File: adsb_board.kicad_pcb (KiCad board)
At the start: 2 copper layers, 3 parts, among them J1 Conn_Coaxial, J2 Conn_Coaxial, U1 TA1090EC

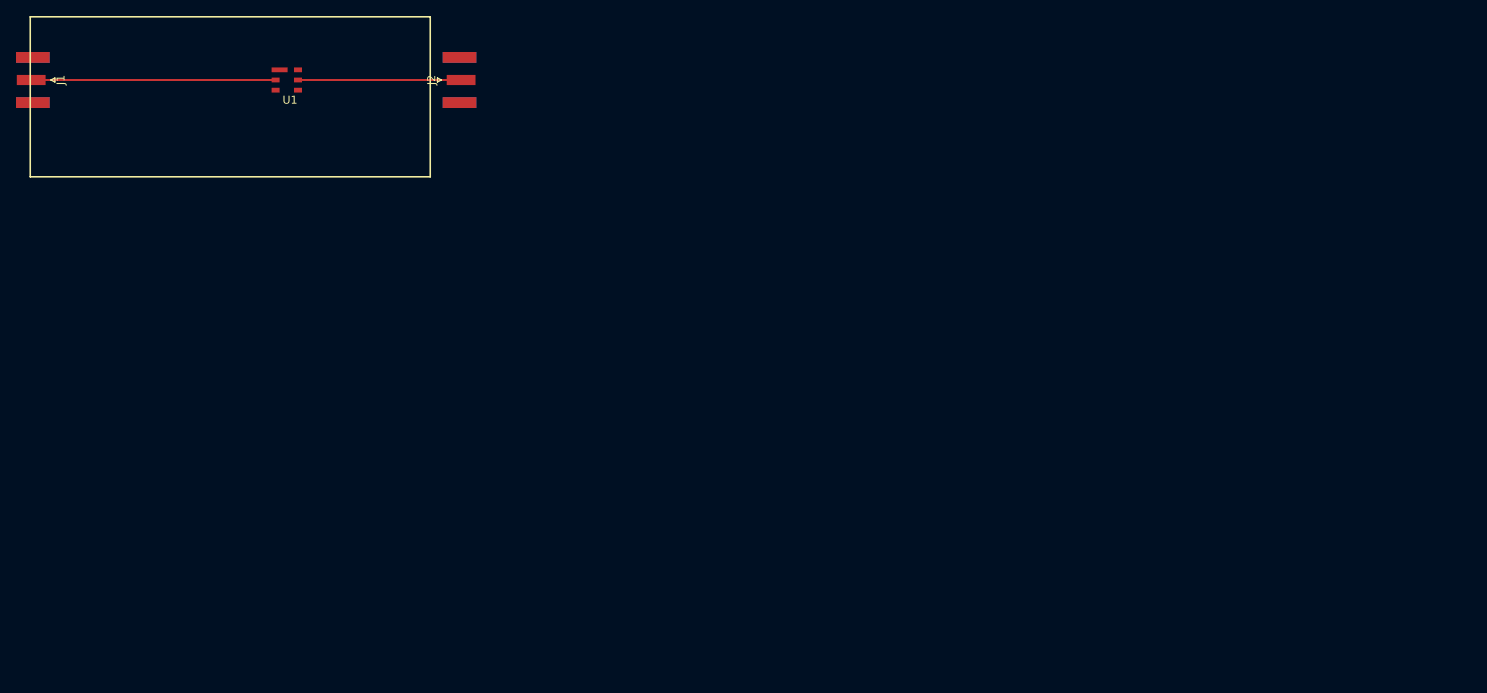
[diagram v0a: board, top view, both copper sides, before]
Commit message: - add four mounting holes m4
- improve layout (with gnd-planes)
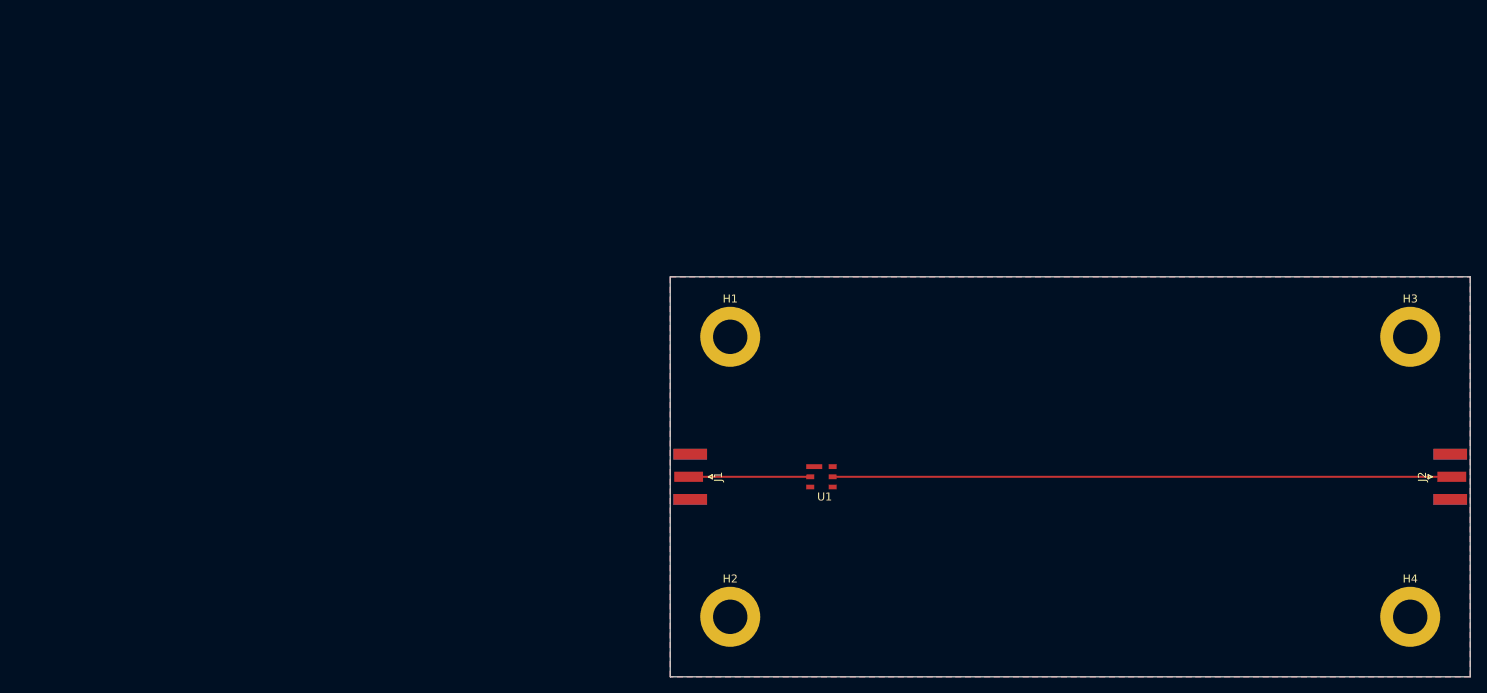
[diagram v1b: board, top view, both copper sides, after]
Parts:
- added H1: MountingHole_Pad, MountingHole:MountingHole_4.3mm_M4_DIN965_Pad, F.Cu at (107.5, 57.5)
- added H2: MountingHole_Pad, MountingHole:MountingHole_4.3mm_M4_DIN965_Pad, F.Cu at (107.5, 92.5)
- added H3: MountingHole_Pad, MountingHole:MountingHole_4.3mm_M4_DIN965_Pad, F.Cu at (192.5, 57.5)
- added H4: MountingHole_Pad, MountingHole:MountingHole_4.3mm_M4_DIN965_Pad, F.Cu at (192.5, 92.5)
- moved J2 133.4 mm to (197.5, 75.0)
- moved J1 96.0 mm to (102.5, 75.0)
- moved U1 83.2 mm to (118.9, 75.0)
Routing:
- net Net-(J2-Pad1): track 20.4 -> 77.4 mm
- net Net-(J1-Pad1): track 30.6 -> 15.2 mm
- added copper zone on B.Cu, net GND
- added copper zone on F.Cu, net GND
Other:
- board outline added: 100 x 50 mm
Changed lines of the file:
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@@
     (tracks 2)
     (zones 0)
-    (modules 3)
+    (modules 7)
     (nets 7)
   )
@@
   (layers
     (0 F.Cu signal)
-    (31 B.Cu signal)
+    (31 B.Cu signal hide)
     (32 B.Adhes user)
     (33 F.Adhes user)
@@
     (add_net "Net-(U1-Pad6)")
   )
-  (module Filter:ta1090ec (layer F.Cu)
-    (at 52.07 25.4)
-    (fp_text reference U1 (at 0.4 2.5) (layer F.SilkS)
-      (effects (font (size 1 1) (thickness 0.15)))
-    )
-    (fp_text value TA1090EC (at 0.4 -2.4) (layer F.Fab)
-      (effects (font (size 1 1) (thickness 0.15)))
-    )
-    (pad 5 smd rect (at 1.4 0) (size 1 0.6) (layers F.Cu F.Paste F.Mask)
-      (net 1 "Net-(J2-Pad1)"))
-    (pad 4 smd rect (at 1.4 1.27) (size 1 0.6) (layers F.Cu F.Paste F.Mask)
-      (net 4 "Net-(U1-Pad4)"))
-    (pad 1 smd rect (at -1.4 -1.27) (size 2 0.6) (drill (offset 0.5 0)) (layers F.Cu F.Paste F.Mask)
-      (net 3 GND))
-    (pad 2 smd rect (at -1.4 0) (size 1 0.6) (layers F.Cu F.Paste F.Mask)
-      (net 2 "Net-(J1-Pad1)"))
-    (pad 3 smd rect (at -1.4 1.27) (size 1 0.6) (layers F.Cu F.Paste F.Mask)
-      (net 5 "Net-(U1-Pad3)"))
-    (pad 6 smd rect (at 1.4 -1.27) (size 1 0.6) (layers F.Cu F.Paste F.Mask)
-      (net 6 "Net-(U1-Pad6)"))
-  )
   (module Connector_Coaxial:SMA_Samtec_SMA-J-P-H-ST-EM1_EdgeMount (layer F.Cu)
-    (at 73.66 25.4)
+    (at 197.5 75)
     (descr http://suddendocs.samtec.com/prints/sma-j-p-x-st-em1-mkt.pdf)
     (tags SMA)
@@
   )
   (module Connector_Coaxial:SMA_Samtec_SMA-J-P-H-ST-EM1_EdgeMount (layer F.Cu)
-    (at 20.32 25.4 180)
+    (at 102.5 75 180)
     (descr http://suddendocs.samtec.com/prints/sma-j-p-x-st-em1-mkt.pdf)
     (tags SMA)
@@
     )
   )
-  (gr_line (start 20 17.5) (end 20 37.5) (layer F.SilkS) (width 0.2))
-  (gr_line (start 70 17.5) (end 20 17.5) (layer F.SilkS) (width 0.2))
-  (gr_line (start 70 37.5) (end 70 17.5) (layer F.SilkS) (width 0.2))
-  (gr_line (start 20 37.5) (end 70 37.5) (layer F.SilkS) (width 0.2))
-  (segment (start 73.86 25.4) (end 53.47 25.4) (width 0.25) (layer F.Cu) (net 1))
-  (segment (start 50.67 25.4) (end 20.12 25.4) (width 0.25) (layer F.Cu) (net 2))
+  (module Filter:ta1090ec (layer F.Cu)
+    (at 118.9 75)
+    (fp_text reference U1 (at 0.4 2.5) (layer F.SilkS)
+      (effects (font (size 1 1) (thickness 0.15)))
+    )
+    (fp_text value TA1090EC (at 0.4 -2.4) (layer F.Fab)
+      (effects (font (size 1 1) (thickness 0.15)))
+    )
+    (pad 5 smd rect (at 1.4 0) (size 1 0.6) (layers F.Cu F.Paste F.Mask)
+      (net 1 "Net-(J2-Pad1)"))
+    (pad 4 smd rect (at 1.4 1.27) (size 1 0.6) (layers F.Cu F.Paste F.Mask)
+      (net 4 "Net-(U1-Pad4)"))
+    (pad 1 smd rect (at -1.4 -1.27) (size 2 0.6) (drill (offset 0.5 0)) (layers F.Cu F.Paste F.Mask)
+      (net 3 GND))
+    (pad 2 smd rect (at -1.4 0) (size 1 0.6) (layers F.Cu F.Paste F.Mask)
+      (net 2 "Net-(J1-Pad1)"))
+    (pad 3 smd rect (at -1.4 1.27) (size 1 0.6) (layers F.Cu F.Paste F.Mask)
+      (net 5 "Net-(U1-Pad3)"))
+    (pad 6 smd rect (at 1.4 -1.27) (size 1 0.6) (layers F.Cu F.Paste F.Mask)
+      (net 6 "Net-(U1-Pad6)"))
+  )
+  (module MountingHole:MountingHole_4.3mm_M4_DIN965_Pad (layer F.Cu)
+    (at 192.5 92.5)
+    (descr "Mounting Hole 4.3mm, M4, DIN965")
+    (tags "mounting hole 4.3mm m4 din965")
+    (attr virtual)
+    (fp_text reference H4 (at 0 -4.75) (layer F.SilkS)
+      (effects (font (size 1 1) (thickness 0.15)))
+    )
+    (fp_text value MountingHole_Pad (at 0 4.75) (layer F.Fab)
+      (effects (font (size 1 1) (thickness 0.15)))
+    )
+    (fp_circle (center 0 0) (end 4 0) (layer F.CrtYd) (width 0.05))
+    (fp_circle (center 0 0) (end 3.75 0) (layer Cmts.User) (width 0.15))
+    (fp_text user %R (at 0.3 0) (layer F.Fab)
+      (effects (font (size 1 1) (thickness 0.15)))
+    )
+    (pad 1 thru_hole circle (at 0 0) (size 7.5 7.5) (drill 4.3) (layers *.Cu *.Mask)
+      (net 3 GND))
+  )
+  (module MountingHole:MountingHole_4.3mm_M4_DIN965_Pad (layer F.Cu)
+    (at 192.5 57.5)
+    (descr "Mounting Hole 4.3mm, M4, DIN965")
+    (tags "mounting hole 4.3mm m4 din965")
+    (attr virtual)
+    (fp_text reference H3 (at 0 -4.75) (layer F.SilkS)
+      (effects (font (size 1 1) (thickness 0.15)))
+    )
+    (fp_text value MountingHole_Pad (at 0 4.75) (layer F.Fab)
+      (effects (font (size 1 1) (thickness 0.15)))
+    )
+    (fp_text user %R (at 0.3 0) (layer F.Fab)
+      (effects (font (size 1 1) (thickness 0.15)))
+    )
+    (fp_circle (center 0 0) (end 3.75 0) (layer Cmts.User) (width 0.15))
+    (fp_circle (center 0 0) (end 4 0) (layer F.CrtYd) (width 0.05))
+    (pad 1 thru_hole circle (at 0 0) (size 7.5 7.5) (drill 4.3) (layers *.Cu *.Mask)
+      (net 3 GND))
+  )
+  (module MountingHole:MountingHole_4.3mm_M4_DIN965_Pad (layer F.Cu)
+    (at 107.5 92.5)
+    (descr "Mounting Hole 4.3mm, M4, DIN965")
+    (tags "mounting hole 4.3mm m4 din965")
+    (attr virtual)
+    (fp_text reference H2 (at 0 -4.75) (layer F.SilkS)
+      (effects (font (size 1 1) (thickness 0.15)))
+    )
+    (fp_text value MountingHole_Pad (at 0 4.75) (layer F.Fab)
+      (effects (font (size 1 1) (thickness 0.15)))
+    )
+    (fp_circle (center 0 0) (end 4 0) (layer F.CrtYd) (width 0.05))
+    (fp_circle (center 0 0) (end 3.75 0) (layer Cmts.User) (width 0.15))
+    (fp_text user %R (at 0.3 0) (layer F.Fab)
+      (effects (font (size 1 1) (thickness 0.15)))
+    )
+    (pad 1 thru_hole circle (at 0 0) (size 7.5 7.5) (drill 4.3) (layers *.Cu *.Mask)
+      (net 3 GND))
+  )
+  (module MountingHole:MountingHole_4.3mm_M4_DIN965_Pad (layer F.Cu)
+    (at 107.5 57.5)
+    (descr "Mounting Hole 4.3mm, M4, DIN965")
+    (tags "mounting hole 4.3mm m4 din965")
+    (attr virtual)
+    (fp_text reference H1 (at 0 -4.75) (layer F.SilkS)
+      (effects (font (size 1 1) (thickness 0.15)))
+    )
+    (fp_text value MountingHole_Pad (at 0 4.75) (layer F.Fab)
+      (effects (font (size 1 1) (thickness 0.15)))
+    )
+    (fp_text user %R (at 0.3 0) (layer F.Fab)
+      (effects (font (size 1 1) (thickness 0.15)))
+    )
+    (fp_circle (center 0 0) (end 3.75 0) (layer Cmts.User) (width 0.15))
+    (fp_circle (center 0 0) (end 4 0) (layer F.CrtYd) (width 0.05))
+    (pad 1 thru_hole circle (at 0 0) (size 7.5 7.5) (drill 4.3) (layers *.Cu *.Mask)
+      (net 3 GND))
+  )
+  (gr_line (start 100 50) (end 100 100) (layer Edge.Cuts) (width 0.15))
+  (gr_line (start 200 50) (end 100 50) (layer Edge.Cuts) (width 0.15))
+  (gr_line (start 200 100) (end 200 50) (layer Edge.Cuts) (width 0.15))
+  (gr_line (start 100 100) (end 200 100) (layer Edge.Cuts) (width 0.15))
+  (segment (start 120.3 75) (end 197.7 75) (width 0.25) (layer F.Cu) (net 1))
+  (segment (start 102.3 75) (end 117.5 75) (width 0.25) (layer F.Cu) (net 2))
+  (zone (net 3) (net_name GND) (layer F.Cu) (hatch edge 0.508)
+    (connect_pads (clearance 0.508))
+    (min_thickness 0.254)
+    (fill yes (arc_segments 16) (thermal_gap 0.508) (thermal_bridge_width 0.508))
+    (polygon
+      (pts
+        (xy 100 50) (xy 200 50) (xy 200 100) (xy 100 100)
+      )
+    )
+  )
+  (zone (net 3) (net_name GND) (layer B.Cu) (hatch edge 0.508)
+    (connect_pads (clearance 0.508))
+    (min_thickness 0.254)
+    (fill yes (arc_segments 16) (thermal_gap 0.508) (thermal_bridge_width 0.508))
+    (polygon
+      (pts
+        (xy 200 50) (xy 200 100) (xy 100 100) (xy 100 50)
+      )
+    )
+  )
 )

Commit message: more improvements
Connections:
- U1 pad 3: Net-(U1-Pad3) -> GND
- U1 pad 4: Net-(U1-Pad4) -> GND
- U1 pad 6: Net-(U1-Pad6) -> GND
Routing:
- net GND: track 0.00 -> 0.80 mm
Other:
- board text added: "ADSB-Filter v0.1 2019-03-11 Maurice Guettler"
- board text added: "INPUT"
- board text added: "OUTPUT"
- board text added: "TA1090EC"
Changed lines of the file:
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@@
   (general
     (thickness 1.6)
-    (drawings 4)
-    (tracks 2)
+    (drawings 8)
+    (tracks 4)
     (zones 0)
     (modules 7)
-    (nets 7)
+    (nets 4)
   )
   (page A4)
@@
   (setup
     (last_trace_width 0.25)
+    (user_trace_width 0.3)
+    (user_trace_width 0.4)
+    (user_trace_width 0.5)
+    (user_trace_width 0.75)
+    (user_trace_width 1)
+    (user_trace_width 2)
     (trace_clearance 0.2)
     (zone_clearance 0.508)
@@
       (outputformat 1)
       (mirror false)
-      (drillshape 1)
+      (drillshape 0)
       (scaleselection 1)
-      (outputdirectory ""))
+      (outputdirectory "../../dump/adsb_test_gerber/"))
   )
   (net 0 "")
@@
   (net 2 "Net-(J1-Pad1)")
   (net 3 GND)
-  (net 4 "Net-(U1-Pad4)")
-  (net 5 "Net-(U1-Pad3)")
-  (net 6 "Net-(U1-Pad6)")
   (net_class Default "Dies ist die voreingestellte Netzklasse."
     (clearance 0.2)
@@
     (add_net "Net-(J1-Pad1)")
     (add_net "Net-(J2-Pad1)")
-    (add_net "Net-(U1-Pad3)")
-    (add_net "Net-(U1-Pad4)")
-    (add_net "Net-(U1-Pad6)")
   )
   (module Connector_Coaxial:SMA_Samtec_SMA-J-P-H-ST-EM1_EdgeMount (layer F.Cu)
@@
       (net 1 "Net-(J2-Pad1)"))
     (pad 4 smd rect (at 1.4 1.27) (size 1 0.6) (layers F.Cu F.Paste F.Mask)
-      (net 4 "Net-(U1-Pad4)"))
+      (net 3 GND))
     (pad 1 smd rect (at -1.4 -1.27) (size 2 0.6) (drill (offset 0.5 0)) (layers F.Cu F.Paste F.Mask)
       (net 3 GND))
@@
       (net 2 "Net-(J1-Pad1)"))
     (pad 3 smd rect (at -1.4 1.27) (size 1 0.6) (layers F.Cu F.Paste F.Mask)
-      (net 5 "Net-(U1-Pad3)"))
+      (net 3 GND))
     (pad 6 smd rect (at 1.4 -1.27) (size 1 0.6) (layers F.Cu F.Paste F.Mask)
-      (net 6 "Net-(U1-Pad6)"))
+      (net 3 GND))
   )
   (module MountingHole:MountingHole_4.3mm_M4_DIN965_Pad (layer F.Cu)
@@
       (net 3 GND))
   )
+  (gr_text TA1090EC (at 119 80) (layer F.SilkS)
+    (effects (font (size 1.5 1.5) (thickness 0.3)))
+  )
+  (gr_text OUTPUT (at 191 75 90) (layer F.SilkS)
+    (effects (font (size 1.5 1.5) (thickness 0.3)))
+  )
+  (gr_text INPUT (at 108 75 90) (layer F.SilkS)
+    (effects (font (size 1.5 1.5) (thickness 0.3)))
+  )
+  (gr_text "ADSB-Filter v0.1\n2019-03-11\nMaurice Guettler" (at 117 58) (layer F.SilkS)
+    (effects (font (size 1.5 1.5) (thickness 0.3)) (justify left))
+  )
   (gr_line (start 100 50) (end 100 100) (layer Edge.Cuts) (width 0.15))
   (gr_line (start 200 50) (end 100 50) (layer Edge.Cuts) (width 0.15))
@@
   (segment (start 120.3 75) (end 197.7 75) (width 0.25) (layer F.Cu) (net 1))
   (segment (start 102.3 75) (end 117.5 75) (width 0.25) (layer F.Cu) (net 2))
+  (segment (start 120.3 73.18) (end 120.48 73) (width 0.25) (layer F.Cu) (net 3))
+  (segment (start 120.3 73.73) (end 120.3 73.18) (width 0.25) (layer F.Cu) (net 3))
   (zone (net 3) (net_name GND) (layer F.Cu) (hatch edge 0.508)
     (connect_pads (clearance 0.508))

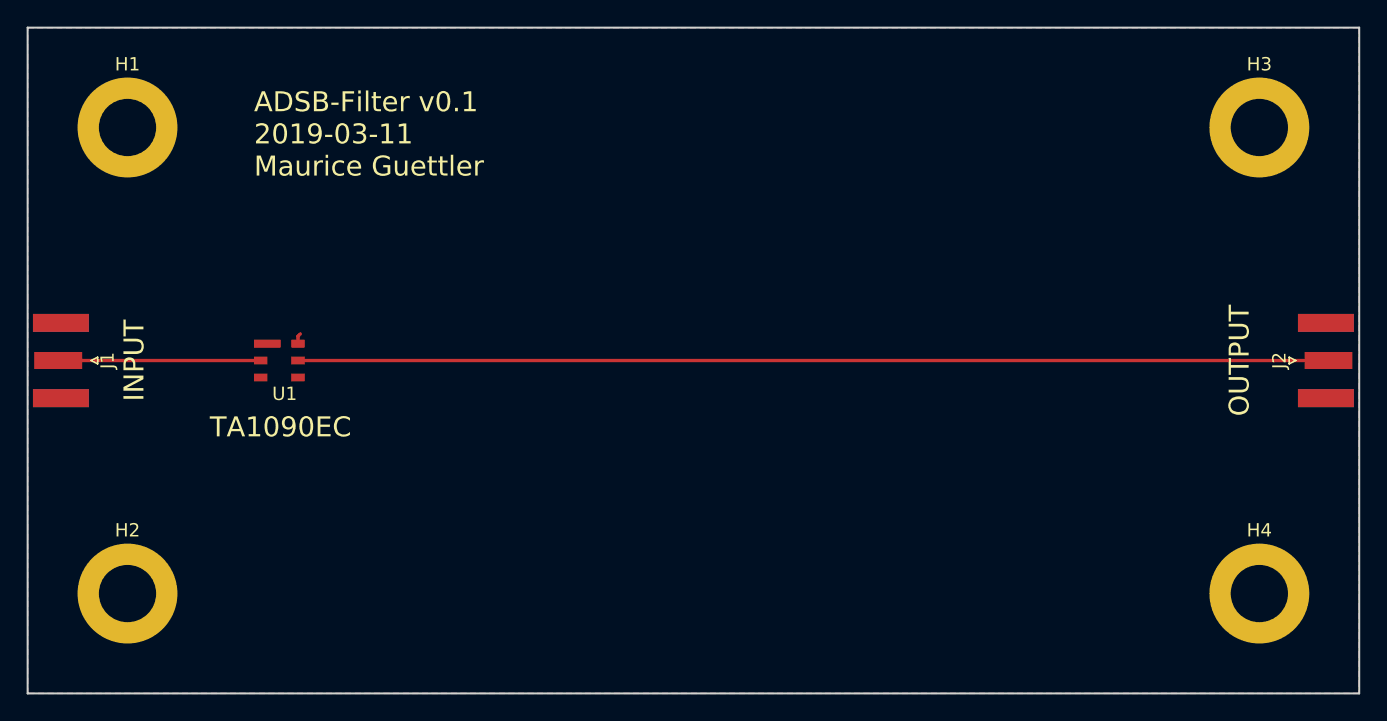
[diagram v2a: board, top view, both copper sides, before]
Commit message: change board size to 50x50mm
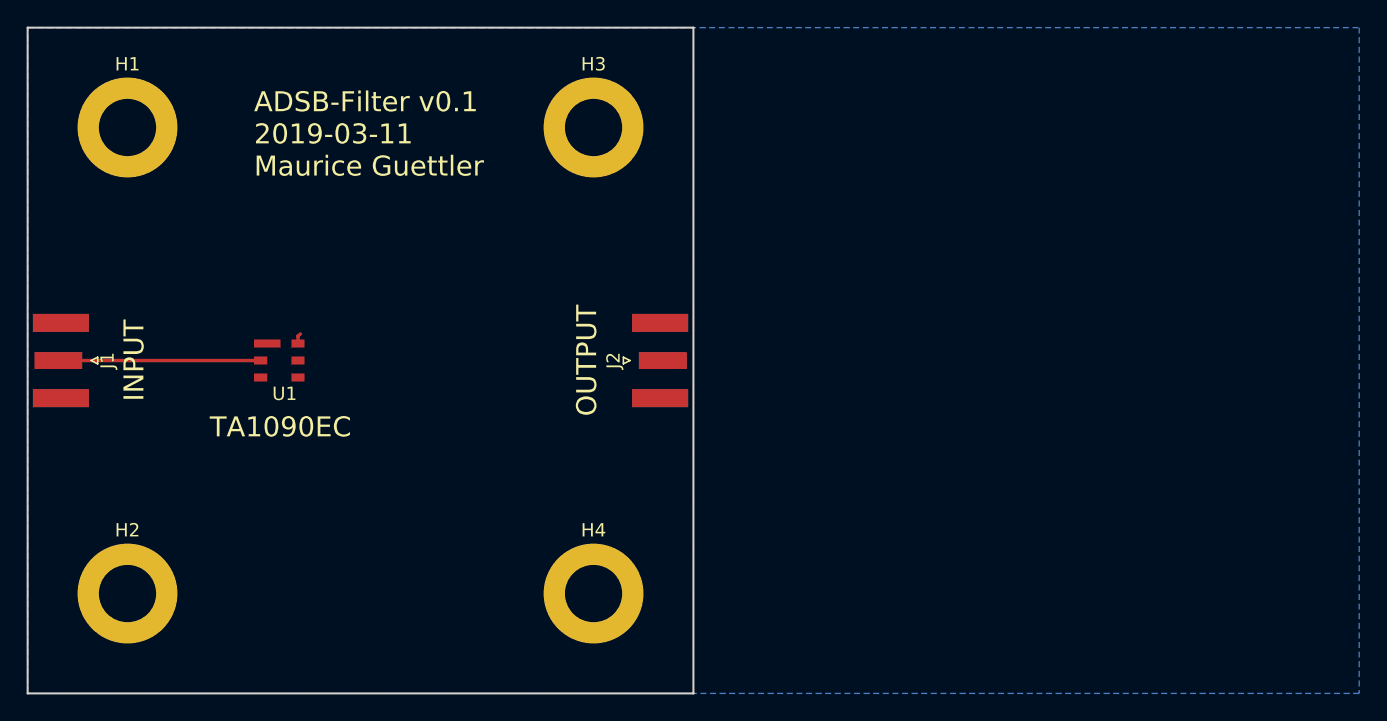
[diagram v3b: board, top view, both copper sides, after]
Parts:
- moved H3 50.0 mm to (142.5, 57.5)
- moved H4 50.0 mm to (142.5, 92.5)
- moved J2 50.0 mm to (147.5, 75.0)
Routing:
- net Net-(J2-Pad1): track 77.4 -> 0.00 mm
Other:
- board size 100 x 50 mm -> 50 x 50 mm
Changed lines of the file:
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@@
     (thickness 1.6)
     (drawings 8)
-    (tracks 4)
+    (tracks 3)
     (zones 0)
     (modules 7)
@@
   )
   (module Connector_Coaxial:SMA_Samtec_SMA-J-P-H-ST-EM1_EdgeMount (layer F.Cu)
-    (at 197.5 75)
+    (at 147.5 75)
     (descr http://suddendocs.samtec.com/prints/sma-j-p-x-st-em1-mkt.pdf)
     (tags SMA)
@@
   )
   (module MountingHole:MountingHole_4.3mm_M4_DIN965_Pad (layer F.Cu)
-    (at 192.5 92.5)
+    (at 142.5 92.5)
     (descr "Mounting Hole 4.3mm, M4, DIN965")
     (tags "mounting hole 4.3mm m4 din965")
@@
   )
   (module MountingHole:MountingHole_4.3mm_M4_DIN965_Pad (layer F.Cu)
-    (at 192.5 57.5)
+    (at 142.5 57.5)
     (descr "Mounting Hole 4.3mm, M4, DIN965")
     (tags "mounting hole 4.3mm m4 din965")
@@
     (effects (font (size 1.5 1.5) (thickness 0.3)))
   )
-  (gr_text OUTPUT (at 191 75 90) (layer F.SilkS)
+  (gr_text OUTPUT (at 142 75 90) (layer F.SilkS)
     (effects (font (size 1.5 1.5) (thickness 0.3)))
   )
@@
   )
   (gr_line (start 100 50) (end 100 100) (layer Edge.Cuts) (width 0.15))
-  (gr_line (start 200 50) (end 100 50) (layer Edge.Cuts) (width 0.15))
-  (gr_line (start 200 100) (end 200 50) (layer Edge.Cuts) (width 0.15))
-  (gr_line (start 100 100) (end 200 100) (layer Edge.Cuts) (width 0.15))
-  (segment (start 120.3 75) (end 197.7 75) (width 0.25) (layer F.Cu) (net 1))
+  (gr_line (start 150 50) (end 100 50) (layer Edge.Cuts) (width 0.15))
+  (gr_line (start 150 100) (end 150 50) (layer Edge.Cuts) (width 0.15))
+  (gr_line (start 100 100) (end 150 100) (layer Edge.Cuts) (width 0.15))
   (segment (start 102.3 75) (end 117.5 75) (width 0.25) (layer F.Cu) (net 2))
   (segment (start 120.3 73.18) (end 120.48 73) (width 0.25) (layer F.Cu) (net 3))
@@
     (polygon
       (pts
-        (xy 100 50) (xy 200 50) (xy 200 100) (xy 100 100)
+        (xy 100 50) (xy 150 50) (xy 150 100) (xy 100 100)
       )
     )
